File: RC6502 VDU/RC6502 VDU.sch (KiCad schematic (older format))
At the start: 35 parts, among them J1 RC6502_Backplane, J2 VDU_BASE, J3 VIDEO, J4 Hole, J5 Hole, J6 Hole, J7 Hole, J8 RCA_PLUG, U1 MC6847, U10 74LS02, U11 VDU_Port, U12 74LS374, U2 HM62256BLP-7, U3 74LS244, U4 74LS244, U5 74LS245, U6 74LS374, U7 74HCT138, U8 74LS32, U9 74HCT138, X1 3.579545 MHz

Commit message: VDU PCB layout done
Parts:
- J2: footprint Pin_Headers:Pin_Header_Straight_2x05_Pitch2.54mm -> Pin_Headers:Pin_Header_Straight_2x07_Pitch2.54mm; symbol Conn_02x05_Odd_Even -> Conn_02x07_Odd_Even
- U11: footprint vdu_amplifier:VDU Module -> vdu_amplifier:Amplifier
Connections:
- net VDU_BASE: now also J2.12 (Pin_12), J2.14 (Pin_14)
- net at U7.10 (O5): now also J2.11 (Pin_11)
- net at U7.9 (O6): now also J2.13 (Pin_13)
- no-connect marks 30 -> 28
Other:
- note added: "$D000"
- note added: "$E000"
- note removed: "PIA"
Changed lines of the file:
@@
 Text GLabel 10250 5050 0    60   BiDi ~ 0
 D0
-NoConn ~ 2100 1225
-$Comp
-L Conn_02x05_Odd_Even J2
+$Comp
+L Conn_02x07_Odd_Even J2
 U 1 1 5C0413AA
-P 2600 925
-F 0 "J2" H 2650 1225 50  0000 C CNN
+P 2600 1025
+F 0 "J2" H 2650 1325 50  0000 C CNN
 F 1 "VDU_BASE" H 2650 625 50  0000 C CNN
-F 2 "Pin_Headers:Pin_Header_Straight_2x05_Pitch2.54mm" H 2600 925 50  0001 C CNN
-F 3 "" H 2600 925 50  0001 C CNN
-	1    2600 925
+F 2 "Pin_Headers:Pin_Header_Straight_2x07_Pitch2.54mm" H 2600 1025 50  0001 C CNN
+F 3 "" H 2600 1025 50  0001 C CNN
+	1    2600 1025
 	1    0    0    -1
 $EndComp
@@
 Wire Wire Line
 	2100 1125 2400 1125
-NoConn ~ 2100 1325
 NoConn ~ 2100 1425
 Wire Wire Line
 	2900 725  3300 725
 Wire Wire Line
-	2975 725  2975 1125
+	2975 725  2975 1325
 Wire Wire Line
 	2975 1125 2900 1125
@@
 	2900 825  2975 825
 Connection ~ 2975 825
-Text Notes 2125 1325 0    60   ~ 0
-ROM
 Text Notes 2125 1425 0    60   ~ 0
 ROM
-Text Notes 2125 1225 0    60   ~ 0
-PIA
 Text Notes 2125 1125 0    60   ~ 0
 $C000
@@
 F 0 "U11" H 1200 2625 60  0000 C CNN
 F 1 "VDU_Port" H 1475 2075 60  0000 C CNN
-F 2 "vdu_amplifier:VDU Module" H 1200 2525 60  0001 C CNN
+F 2 "vdu_amplifier:Amplifier" H 1200 2525 60  0001 C CNN
 F 3 "" H 1200 2525 60  0001 C CNN
 	1    1200 2525
@@
 	1    0    0    -1
 $EndComp
+Wire Wire Line
+	2100 1225 2400 1225
+Wire Wire Line
+	2100 1325 2400 1325
+Text Notes 2125 1225 0    60   ~ 0
+$D000
+Text Notes 2125 1325 0    60   ~ 0
+$E000
+Wire Wire Line
+	2975 1225 2900 1225
+Connection ~ 2975 1125
+Wire Wire Line
+	2975 1325 2900 1325
+Connection ~ 2975 1225
 $EndSCHEMATC

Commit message: Cleaned up silkscreen
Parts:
- U3, U4, U5, U6: footprint Housings_DIP:DIP-20_W7.62mm -> Housings_DIP:DIP-20_W7.62mm_Socket
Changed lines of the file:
@@
 F 0 "U4" H 8350 3325 50  0000 C CNN
 F 1 "74LS244" H 8350 3725 50  0000 C CNN
-F 2 "Housings_DIP:DIP-20_W7.62mm" H 8350 3525 50  0001 C CNN
+F 2 "Housings_DIP:DIP-20_W7.62mm_Socket" H 8350 3525 50  0001 C CNN
 F 3 "" H 8350 3525 50  0001 C CNN
 	1    8350 3525
@@
 F 0 "U3" H 8350 2150 50  0000 C CNN
 F 1 "74LS244" H 8350 2550 50  0000 C CNN
-F 2 "Housings_DIP:DIP-20_W7.62mm" H 8350 2350 50  0001 C CNN
+F 2 "Housings_DIP:DIP-20_W7.62mm_Socket" H 8350 2350 50  0001 C CNN
 F 3 "" H 8350 2350 50  0001 C CNN
 	1    8350 2350
@@
 F 0 "U5" H 8350 4950 50  0000 C BNN
 F 1 "74LS245" H 8350 4550 50  0000 C CNN
-F 2 "Housings_DIP:DIP-20_W7.62mm" H 8350 4750 50  0001 C CNN
+F 2 "Housings_DIP:DIP-20_W7.62mm_Socket" H 8350 4750 50  0001 C CNN
 F 3 "" H 8350 4750 50  0001 C CNN
 	1    8350 4750
@@
 F 0 "U6" H 8350 5850 50  0000 C CNN
 F 1 "74LS374" H 8350 6050 50  0000 C CNN
-F 2 "Housings_DIP:DIP-20_W7.62mm" H 8350 5950 50  0001 C CNN
+F 2 "Housings_DIP:DIP-20_W7.62mm_Socket" H 8350 5950 50  0001 C CNN
 F 3 "" H 8350 5950 50  0001 C CNN
 	1    8350 5950

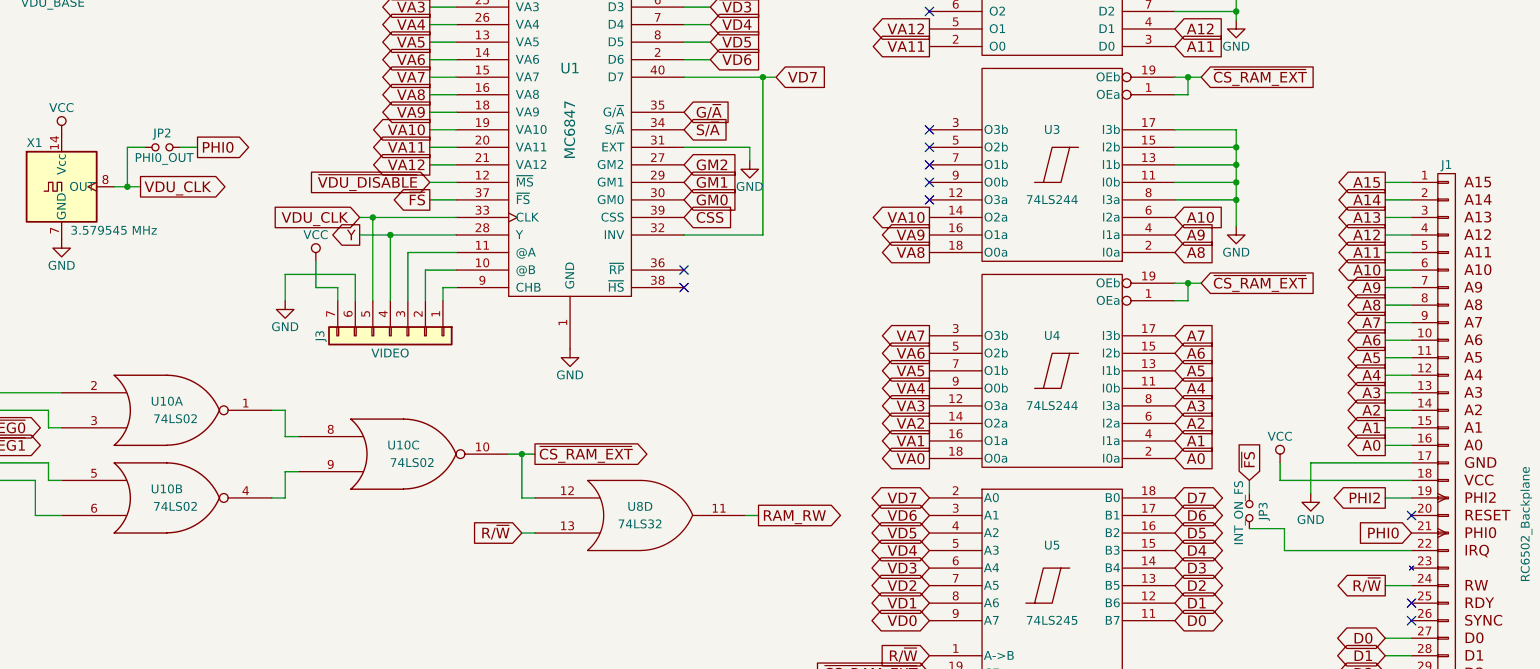
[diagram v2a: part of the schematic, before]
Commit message: Tried to increase ground plane flow
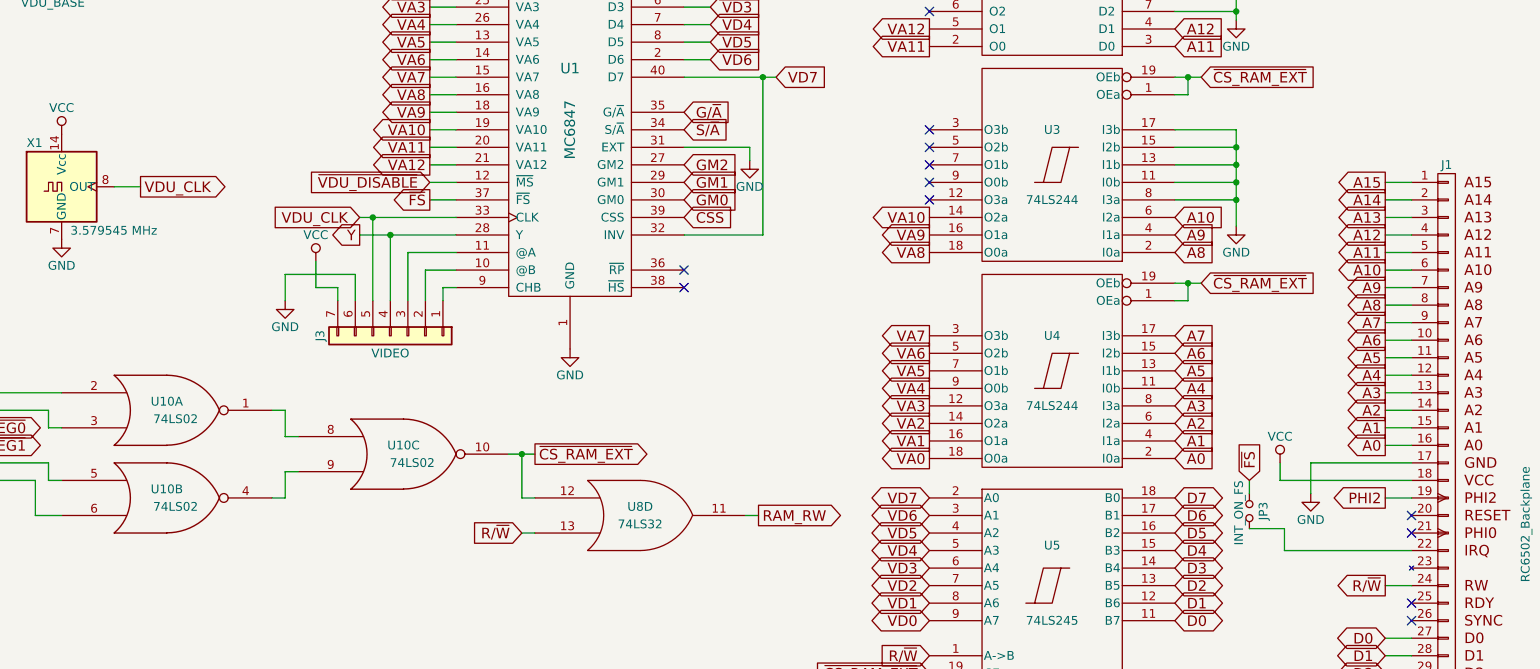
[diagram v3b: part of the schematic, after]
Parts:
- removed JP2: PHI0_OUT, Pin_Headers:Pin_Header_Straight_1x02_Pitch2.54mm, symbol Jumper_NO_Small
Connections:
- net PHI0: no longer names the net of J1.21 (PHI0)
- no-connect marks 28 -> 29
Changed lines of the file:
@@
 Text GLabel 3150 2475 2    60   Output ~ 0
 VDU_CLK
-Wire Wire Line
-	3000 2475 3150 2475
 $Comp
 L GND #PWR02
@@
 Wire Wire Line
 	7500 6450 7650 6450
-Text GLabel 10400 4450 0    60   Input ~ 0
-PHI0
-$Comp
-L Jumper_NO_Small JP2
-U 1 1 5C05E5BB
-P 3275 2250
-F 0 "JP2" H 3275 2330 50  0000 C CNN
-F 1 "PHI0_OUT" H 3285 2190 50  0000 C CNN
-F 2 "Pin_Headers:Pin_Header_Straight_1x02_Pitch2.54mm" H 3275 2250 50  0001 C CNN
-F 3 "" H 3275 2250 50  0001 C CNN
-	1    3275 2250
-	1    0    0    -1
-$EndComp
-Wire Wire Line
-	3075 2475 3075 2250
-Connection ~ 3075 2475
-Wire Wire Line
-	3075 2250 3175 2250
-Text GLabel 3475 2250 2    60   Output ~ 0
-PHI0
-Wire Wire Line
-	3375 2250 3475 2250
 $Comp
 L GND #PWR08
@@
 	2975 1325 2900 1325
 Connection ~ 2975 1225
+Wire Wire Line
+	3000 2475 3150 2475
+NoConn ~ 10400 4450
 $EndSCHEMATC

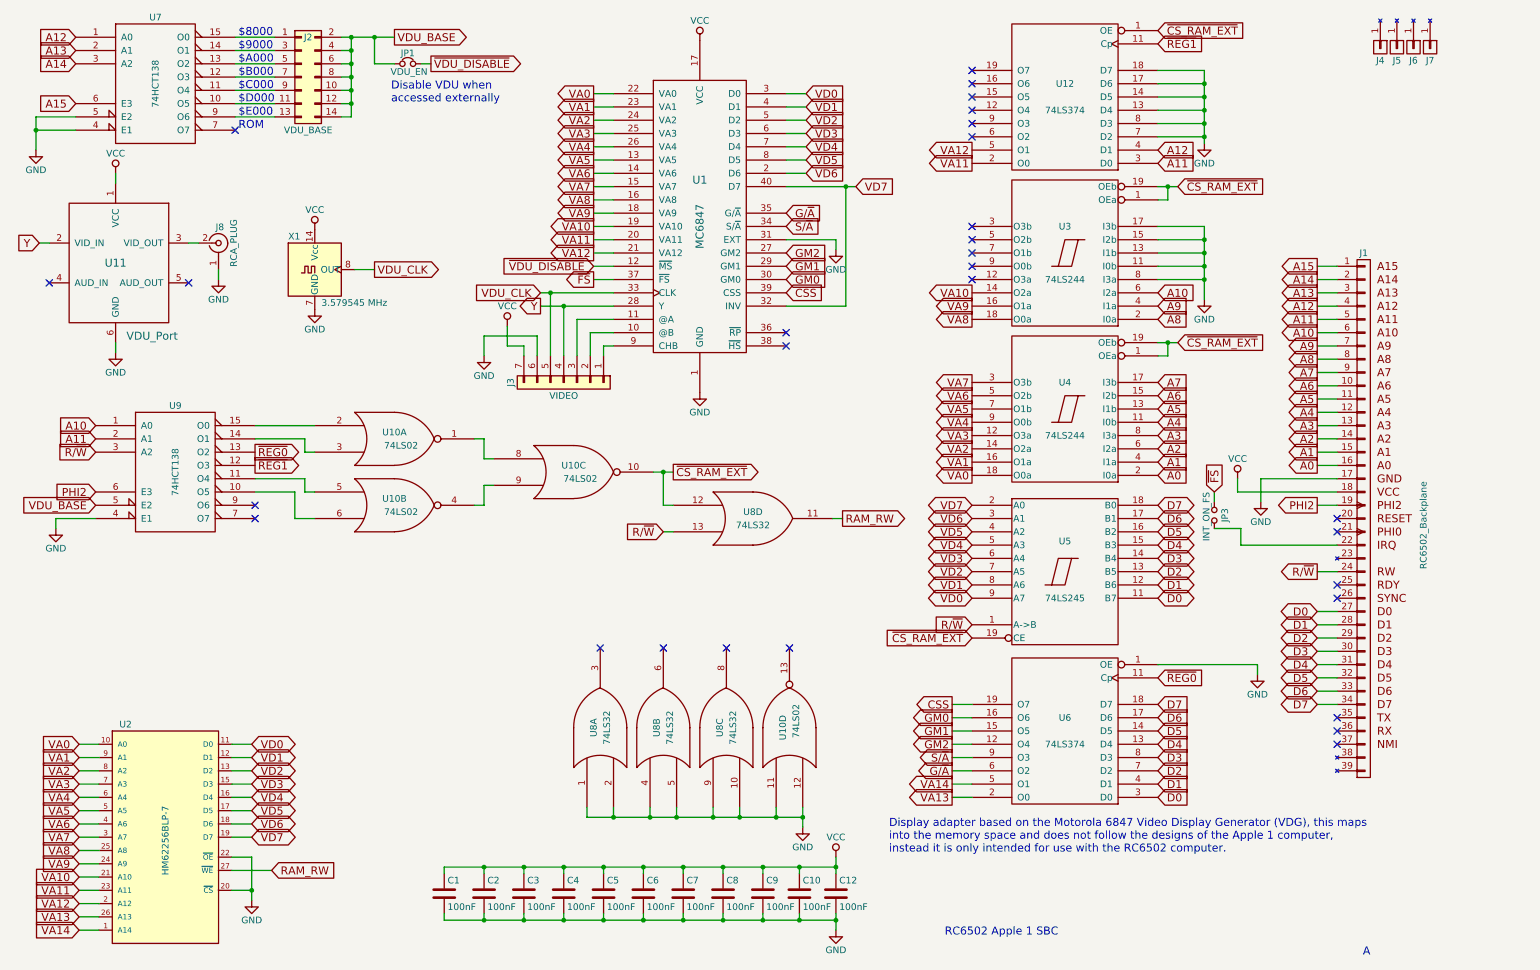
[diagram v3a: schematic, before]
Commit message: Updated VDU schematic with rev. B fixes
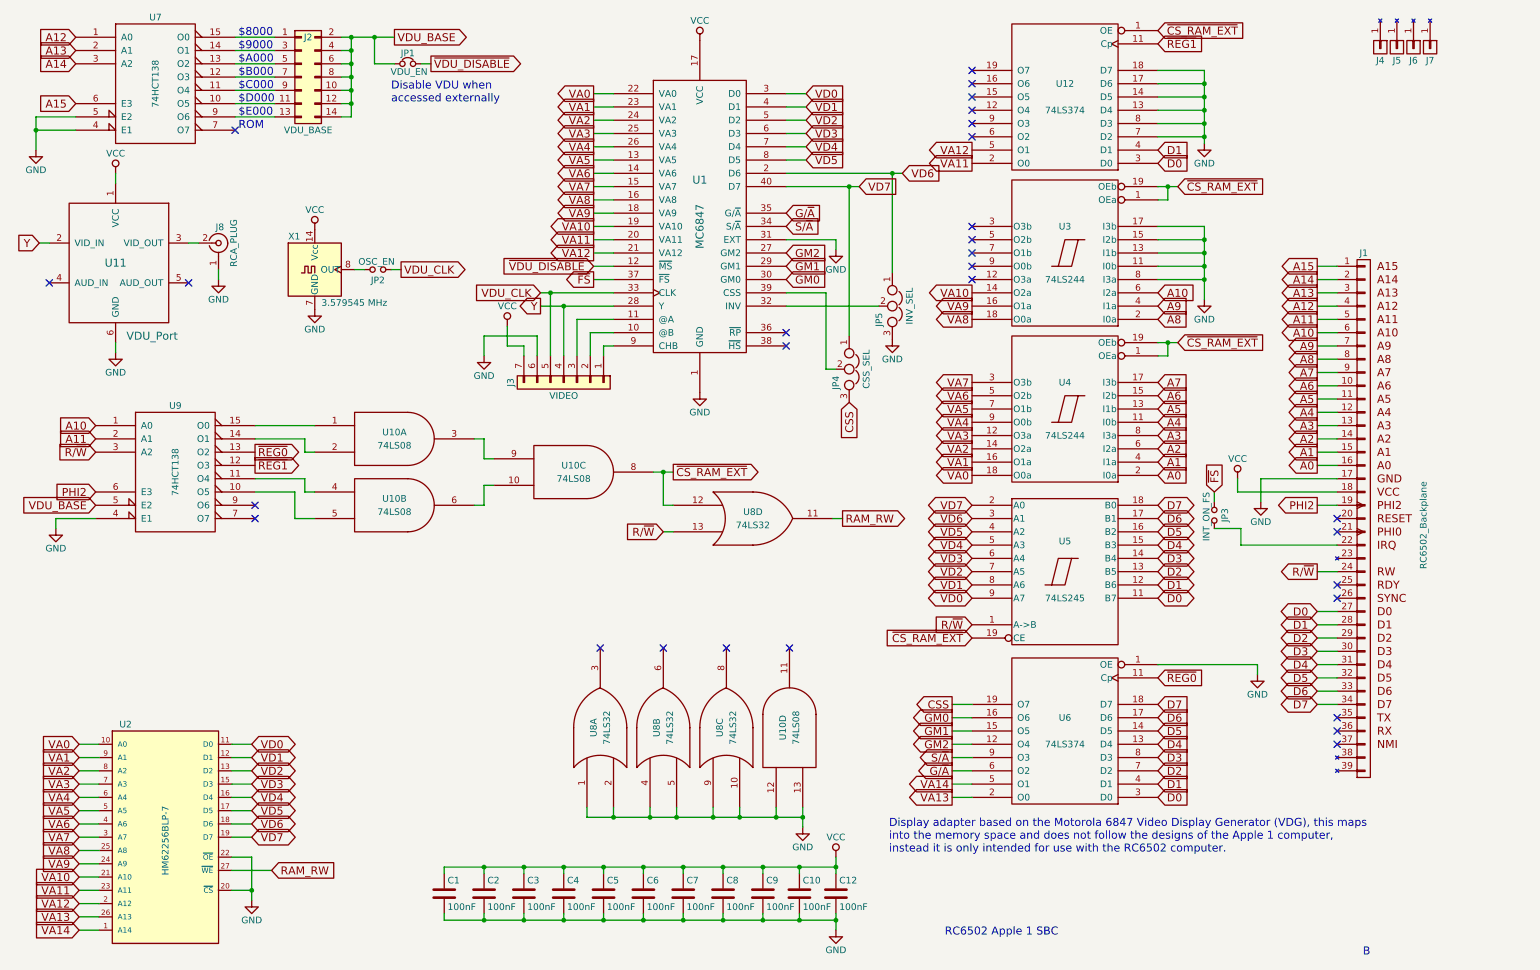
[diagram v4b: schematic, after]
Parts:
- removed U10: 74LS02, Housings_DIP:DIP-14_W7.62mm_Socket, symbol 74LS02
- added JP2: OSC_EN, Pin_Headers:Pin_Header_Straight_1x02_Pitch2.54mm, symbol Jumper_NO_Small
- added JP4: CSS_SEL, Pin_Headers:Pin_Header_Straight_1x03_Pitch2.54mm, symbol Jumper_NC_Dual
- added JP5: INV_SEL, Pin_Headers:Pin_Header_Straight_1x03_Pitch2.54mm, symbol Jumper_NC_Dual
- added U10: 74LS08, Housings_DIP:DIP-14_W7.62mm_Socket, symbol 74LS08
- U12: footprint Housings_DIP:DIP-20_W7.62mm -> Housings_DIP:DIP-20_W7.62mm_Socket
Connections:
- net A11: no longer U12.3 (D0)
- net A12: no longer U12.4 (D1)
- net CSS: now also JP4.3; no longer U1.39 (CSS)
- net D0: now also U12.3 (D0)
- net D1: now also U12.4 (D1)
- net GND: now also JP5.3, U10.12, U10.13, U10.7 (GND), U10.7 (GND), U10.7 (GND), U10.7 (GND)
- net VCC: now also U10.14 (VCC), U10.14 (VCC), U10.14 (VCC), U10.14 (VCC)
- net VD6: now also JP5.1
- net VD7: now also JP4.1; no longer U1.32 (INV)
- net VDU_CLK: now also JP2.1; no longer X1.8 (OUT)
- net ~CS_RAM_EXT: now also U10.8
- net at U9.10 (O5): now also U10.5
- net at U9.11 (O4): now also U10.4
- net at U9.14 (O1): now also U10.2
- net at U9.15 (O0): now also U10.1
- new net: JP2.2, X1.8 (OUT)
- new net: JP5.2, U1.32 (INV)
- new net: JP4.2, U1.39 (CSS)
- new net: U10.3, U10.9
- new net: U10.10, U10.6
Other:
- note added: "B"
- note removed: "A"
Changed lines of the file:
@@
 RC6502 Apple 1 SBC
 Text Notes 10650 7650 2    60   ~ 0
-A
+B
 $Comp
 L 74LS138 U7
@@
 Text GLabel 9050 4025 2    60   Input ~ 0
 A0
-Text GLabel 9050 1575 2    60   Input ~ 0
-A12
-Text GLabel 9050 1675 2    60   Input ~ 0
-A11
 Text GLabel 9050 2650 2    60   Input ~ 0
 A10
@@
 Text GLabel 3300 725  2    60   Output ~ 0
 VDU_BASE
-Text GLabel 3150 2475 2    60   Output ~ 0
+Text GLabel 3350 2475 2    60   Output ~ 0
 VDU_CLK
 $Comp
@@
 Wire Wire Line
 	2075 6050 2225 6050
-Text GLabel 6775 1850 2    60   Input ~ 0
+Text GLabel 6800 1850 2    60   Input ~ 0
 VD7
-Text GLabel 6400 1750 2    60   Input ~ 0
+Text GLabel 7125 1750 2    60   Input ~ 0
 VD6
 Text GLabel 6400 1650 2    60   Input ~ 0
@@
 VD0
 Wire Wire Line
-	6250 1750 6400 1750
-Wire Wire Line
-	6250 1850 6775 1850
-Wire Wire Line
 	6250 1650 6400 1650
 Wire Wire Line
@@
 Wire Wire Line
 	6250 2250 6625 2250
-Wire Wire Line
-	6700 1850 6700 2750
-Wire Wire Line
-	6700 2750 6250 2750
-Connection ~ 6700 1850
 Text GLabel 6250 2050 2    60   Input ~ 0
 G/~A
@@
 Text GLabel 6250 2550 2    60   Input ~ 0
 GM0
-Text GLabel 6250 2650 2    60   Input ~ 0
-CSS
 Text GLabel 7500 5750 0    60   Output ~ 0
 CSS
@@
 F 0 "U12" H 8350 1075 50  0000 C CNN
 F 1 "74LS374" H 8350 1275 50  0000 C CNN
-F 2 "Housings_DIP:DIP-20_W7.62mm" H 8350 1175 50  0001 C CNN
+F 2 "Housings_DIP:DIP-20_W7.62mm_Socket" H 8350 1175 50  0001 C CNN
 F 3 "" H 8350 1175 50  0001 C CNN
 	1    8350 1175
@@
 Text GLabel 1050 3650 0    60   Input ~ 0
 A10
-$Comp
-L 74LS02 U10
-U 1 1 5C276516
-P 3300 3750
-F 0 "U10" H 3300 3800 50  0000 C CNN
-F 1 "74LS02" H 3350 3700 50  0000 C CNN
-F 2 "Housings_DIP:DIP-14_W7.62mm_Socket" H 3300 3750 50  0001 C CNN
-F 3 "" H 3300 3750 50  0001 C CNN
-	1    3300 3750
-	1    0    0    -1
-$EndComp
-$Comp
-L 74LS02 U10
-U 2 1 5C2767ED
-P 3300 4250
-F 0 "U10" H 3300 4300 50  0000 C CNN
-F 1 "74LS02" H 3350 4200 50  0000 C CNN
-F 2 "Housings_DIP:DIP-14_W7.62mm_Socket" H 3300 4250 50  0001 C CNN
-F 3 "" H 3300 4250 50  0001 C CNN
-	2    3300 4250
-	1    0    0    -1
-$EndComp
 Wire Wire Line
 	2700 3650 2250 3650
@@
 Wire Wire Line
 	2550 4350 2700 4350
-$Comp
-L 74LS02 U10
-U 3 1 5C277F93
-P 4650 4000
-F 0 "U10" H 4650 4050 50  0000 C CNN
-F 1 "74LS02" H 4700 3950 50  0000 C CNN
-F 2 "Housings_DIP:DIP-14_W7.62mm_Socket" H 4650 4000 50  0001 C CNN
-F 3 "" H 4650 4000 50  0001 C CNN
-	3    4650 4000
-	1    0    0    -1
-$EndComp
 Wire Wire Line
 	3900 4250 3975 4250
@@
 Text GLabel 7650 5150 0    60   Input ~ 0
 R/~W
-$Comp
-L 74LS02 U10
-U 4 1 5C2945AC
-P 6275 5925
-F 0 "U10" H 6275 5975 50  0000 C CNN
-F 1 "74LS02" H 6325 5875 50  0000 C CNN
-F 2 "Housings_DIP:DIP-14_W7.62mm_Socket" H 6275 5925 50  0001 C CNN
-F 3 "" H 6275 5925 50  0001 C CNN
-	4    6275 5925
-	0    -1   -1   0
-$EndComp
 NoConn ~ 6275 5325
 $Comp
@@
 	0    -1   -1   0
 $EndComp
-Wire Wire Line
-	4750 6600 4750 6525
 Connection ~ 6175 6600
 Wire Wire Line
@@
 	2975 1325 2900 1325
 Connection ~ 2975 1225
-Wire Wire Line
-	3000 2475 3150 2475
 NoConn ~ 10400 4450
+$Comp
+L 74LS08 U10
+U 1 1 5C68D5FB
+P 3300 3750
+F 0 "U10" H 3300 3800 50  0000 C CNN
+F 1 "74LS08" H 3300 3700 50  0000 C CNN
+F 2 "Housings_DIP:DIP-14_W7.62mm_Socket" H 3300 3750 50  0001 C CNN
+F 3 "" H 3300 3750 50  0001 C CNN
+	1    3300 3750
+	1    0    0    -1
+$EndComp
+$Comp
+L 74LS08 U10
+U 2 1 5C68D691
+P 3300 4250
+F 0 "U10" H 3300 4300 50  0000 C CNN
+F 1 "74LS08" H 3300 4200 50  0000 C CNN
+F 2 "Housings_DIP:DIP-14_W7.62mm_Socket" H 3300 4250 50  0001 C CNN
+F 3 "" H 3300 4250 50  0001 C CNN
+	2    3300 4250
+	1    0    0    -1
+$EndComp
+$Comp
+L 74LS08 U10
+U 3 1 5C68D787
+P 4650 4000
+F 0 "U10" H 4650 4050 50  0000 C CNN
+F 1 "74LS08" H 4650 3950 50  0000 C CNN
+F 2 "Housings_DIP:DIP-14_W7.62mm_Socket" H 4650 4000 50  0001 C CNN
+F 3 "" H 4650 4000 50  0001 C CNN
+	3    4650 4000
+	1    0    0    -1
+$EndComp
+$Comp
+L 74LS08 U10
+U 4 1 5C68DB32
+P 6275 5925
+F 0 "U10" H 6275 5975 50  0000 C CNN
+F 1 "74LS08" H 6275 5875 50  0000 C CNN
+F 2 "Housings_DIP:DIP-14_W7.62mm_Socket" H 6275 5925 50  0001 C CNN
+F 3 "" H 6275 5925 50  0001 C CNN
+	4    6275 5925
+	0    -1   -1   0
+$EndComp
+Wire Wire Line
+	4750 6525 4750 6600
+Text GLabel 9050 1575 2    60   Input ~ 0
+D1
+Text GLabel 9050 1675 2    60   Input ~ 0
+D0
+$Comp
+L Jumper_NO_Small JP2
+U 1 1 5C6C8809
+P 3175 2475
+F 0 "JP2" H 3175 2555 50  0000 C CNN
+F 1 "OSC_EN" H 3185 2415 50  0000 C CNN
+F 2 "Pin_Headers:Pin_Header_Straight_1x02_Pitch2.54mm" H 3175 2475 50  0001 C CNN
+F 3 "" H 3175 2475 50  0001 C CNN
+	1    3175 2475
+	-1   0    0    1
+$EndComp
+Wire Wire Line
+	3000 2475 3075 2475
+Wire Wire Line
+	3275 2475 3350 2475
+$Comp
+L Jumper_NC_Dual JP5
+U 1 1 5C6D3681
+P 7050 2750
+F 0 "JP5" H 7100 2650 50  0000 L CNN
+F 1 "INV_SEL" H 7050 2850 50  0000 C BNN
+F 2 "Pin_Headers:Pin_Header_Straight_1x03_Pitch2.54mm" H 7050 2750 50  0001 C CNN
+F 3 "" H 7050 2750 50  0001 C CNN
+	1    7050 2750
+	0    1    1    0
+$EndComp
+Wire Wire Line
+	6250 1750 7125 1750
+$Comp
+L GND #PWR022
+U 1 1 5C6D4550
+P 7050 3000
+F 0 "#PWR022" H 7050 2750 50  0001 C CNN
+F 1 "GND" H 7050 2850 50  0000 C CNN
+F 2 "" H 7050 3000 50  0001 C CNN
+F 3 "" H 7050 3000 50  0001 C CNN
+	1    7050 3000
+	1    0    0    -1
+$EndComp
+$Comp
+L Jumper_NC_Dual JP4
+U 1 1 5C6D4975
+P 6725 3225
+F 0 "JP4" H 6775 3125 50  0000 L CNN
+F 1 "CSS_SEL" H 6725 3325 50  0000 C BNN
+F 2 "Pin_Headers:Pin_Header_Straight_1x03_Pitch2.54mm" H 6725 3225 50  0001 C CNN
+F 3 "" H 6725 3225 50  0001 C CNN
+	1    6725 3225
+	0    1    1    0
+$EndComp
+Text GLabel 6725 3475 3    60   Input ~ 0
+CSS
+Wire Wire Line
+	7050 1750 7050 2500
+Connection ~ 7050 1750
+Wire Wire Line
+	6725 2975 6725 1850
+Wire Wire Line
+	6250 1850 6800 1850
+Connection ~ 6725 1850
+Wire Wire Line
+	6950 2750 6250 2750
+Wire Wire Line
+	6625 3225 6550 3225
+Wire Wire Line
+	6550 3225 6550 2650
+Wire Wire Line
+	6550 2650 6250 2650
 $EndSCHEMATC
